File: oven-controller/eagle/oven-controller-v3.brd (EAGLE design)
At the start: 74.2 x 45.7 mm, 53 parts, among them Q1 FDV305N, Q2 FDV305N, Q3 FDV305N, Q4 FDV305N, U1 ARDUINO_SHIELDNOHOLES, U2 MAX31855, U3 MAX31855, U4 MAX31855, U5 MAX31855, U6 MAX31855

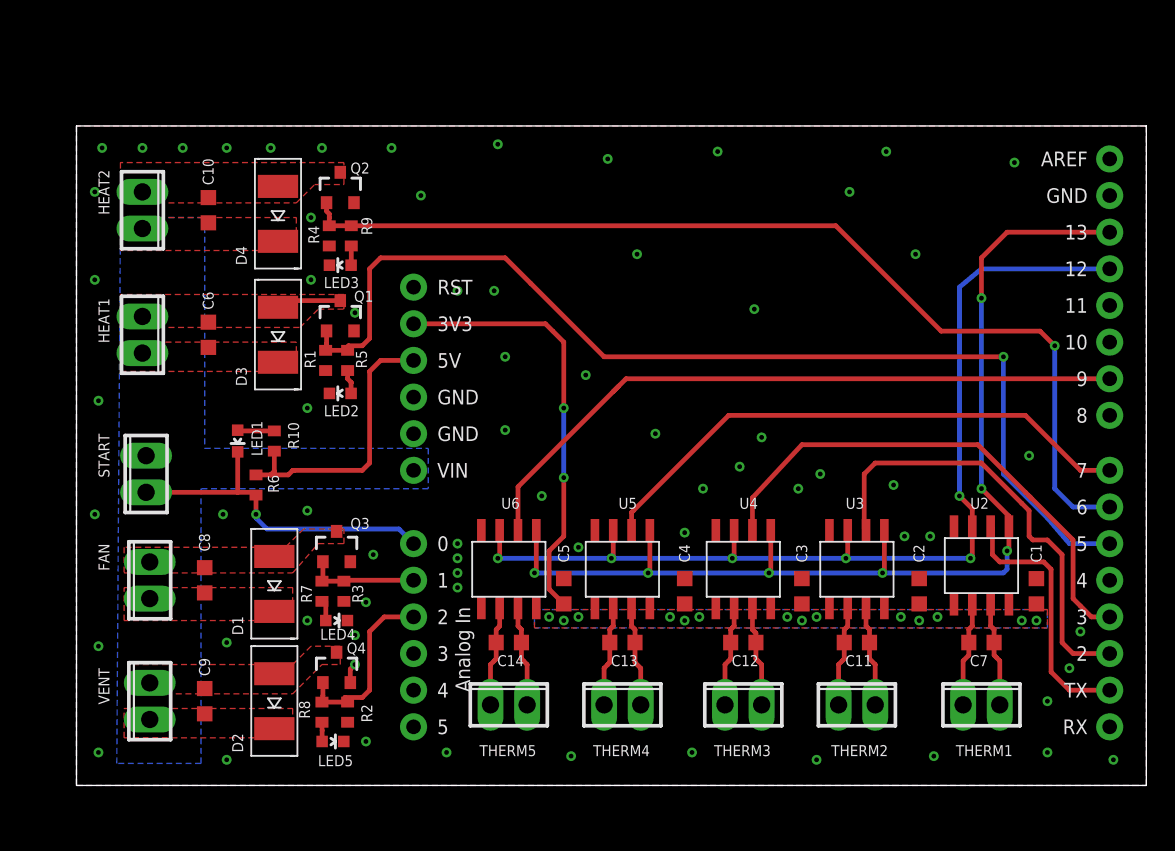
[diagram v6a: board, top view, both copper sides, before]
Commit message: Added level translators. Passes ERC, DRC. Needs review.
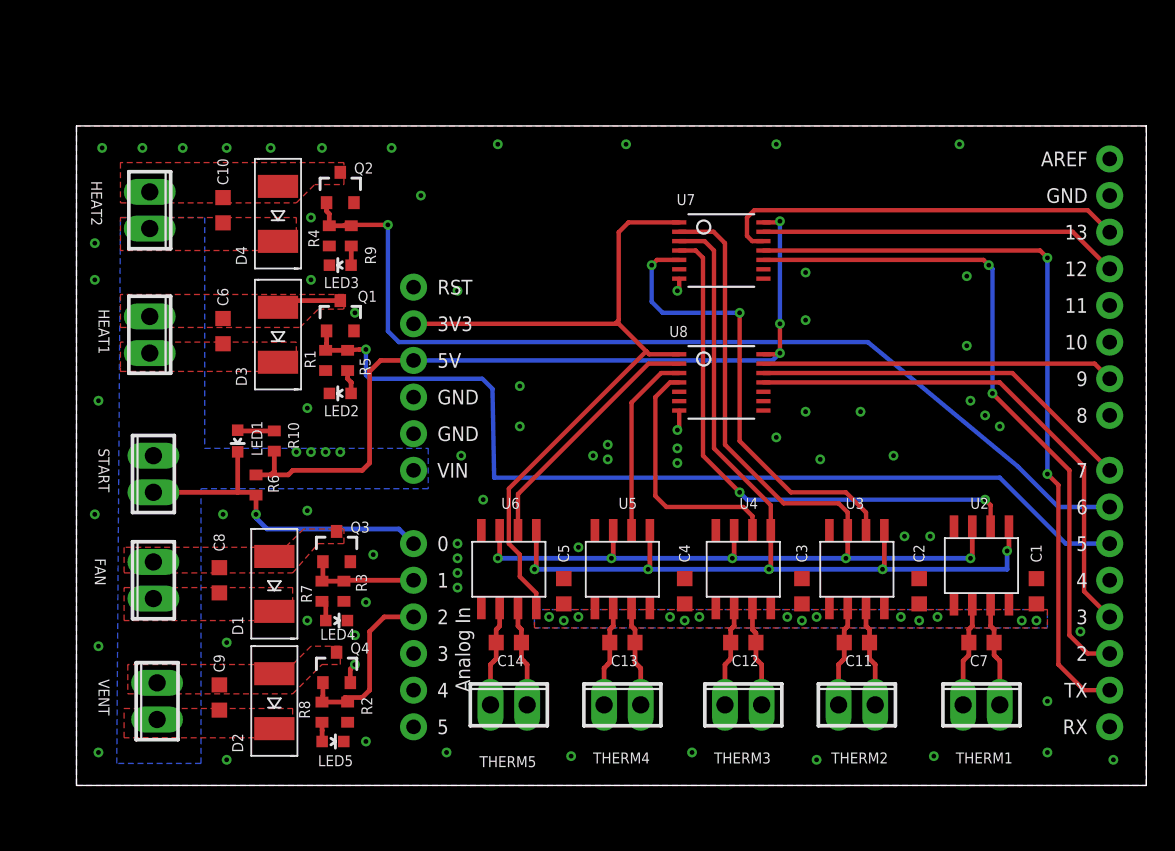
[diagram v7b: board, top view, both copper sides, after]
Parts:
- added U7, U8: (no value), SparkFun-DigitalIC:TSSOP14
- moved C9 1.05 mm to (9.91, 6.10)
- moved C6 1.05 mm to (10.2, 31.5)
- moved C10 1.02 mm to (10.2, 39.9)
- moved C8 1.02 mm to (9.91, 14.2)
- moved HEAT1 0.51 mm to (5.08, 31.2)
- moved HEAT2 0.51 mm to (5.08, 39.9)
- moved START 0.51 mm to (5.33, 21.6)
- moved VENT 0.51 mm to (5.59, 5.84)
- moved FAN 0.25 mm to (5.33, 14.2)
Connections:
- removed net SPI_CLK: U1.D13, U2.5, U3.5, U4.5, U5.5, U6.5
- removed net SPI_MISO: U1.D12, U2.7, U3.7, U4.7, U5.7, U6.7
- removed net THERM_!CS1: U1.TX, U2.6
- removed net THERM_!CS2: U1.D2, U3.6
- removed net THERM_!CS3: U1.D3, U4.6
- removed net THERM_!CS4: U1.D7, U5.6
- removed net THERM_!CS5: U1.D9, U6.6
- new net SPI_CLK_A: U2.5, U3.5, U4.5, U5.5, U6.5, U7.3
- new net SPI_CLK_B: U1.D13, U7.12
- new net SPI_MISO_A: U2.7, U3.7, U4.7, U5.7, U6.7, U7.2
- new net SPI_MISO_B: U1.D12, U7.13
- new net THERM_!CS1_A: U2.6, U7.4
- new net THERM_!CS1_B: U1.TX, U7.11
- new net THERM_!CS2_A: U3.6, U7.5
- new net THERM_!CS2_B: U1.D2, U7.10
- new net THERM_!CS3_A: U4.6, U8.4
- new net THERM_!CS3_B: U1.D3, U8.11
- new net THERM_!CS4_A: U5.6, U8.3
- new net THERM_!CS4_B: U1.D7, U8.12
- new net THERM_!CS5_A: U6.6, U8.2
- new net THERM_!CS5_B: U1.D9, U8.13
- net 3.3V: now also U7.1, U8.1
- net 5V: now also U7.14, U8.14
- net GND: now also U7.7, U8.7
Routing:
- net SPI_CLK: track 77.0 -> 0.00 mm, vias 7 -> 0
- net SPI_MISO_A: track 0.00 -> 72.2 mm, vias 0 -> 5
- net SPI_CLK_A: track 0.00 -> 71.5 mm, vias 0 -> 5
- net SPI_MISO: track 70.9 -> 0.00 mm, vias 6 -> 0
- net THERM_!CS1_B: track 0.00 -> 52.9 mm, vias 0 -> 2
- net THERM_!CS5: track 47.7 -> 0.00 mm
- net THERM_!CS2_B: track 0.00 -> 47.1 mm, vias 0 -> 2
- net THERM_!CS4: track 38.7 -> 0.00 mm
- net THERM_!CS1_A: track 0.00 -> 38.4 mm, vias 0 -> 2
- net 5V: track 19.7 -> 56.8 mm, vias 0 -> 3
- net THERM_!CS3: track 36.1 -> 0.00 mm
- net THERM_!CS3_B: track 0.00 -> 35.8 mm
- net THERM_!CS2_A: track 0.00 -> 31.9 mm, vias 0 -> 2
- net THERM_!CS2: track 31.4 -> 0.00 mm
- net SPI_CLK_B: track 0.00 -> 28.5 mm
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
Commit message: Added v3.1 update to oven board.
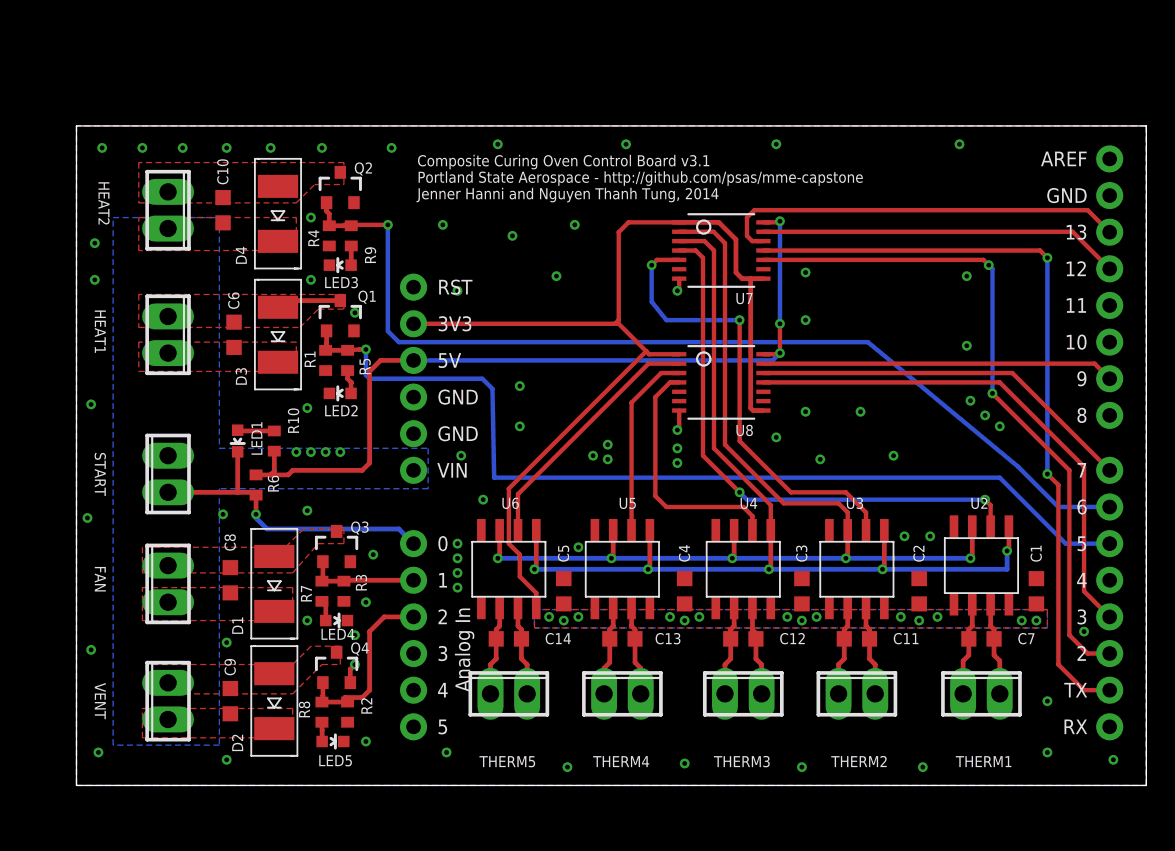
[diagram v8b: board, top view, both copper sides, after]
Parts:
- R10: value 1k -> 150
- U7, U8: value (none) -> TXB0104
- moved HEAT1 1.27 mm to (6.35, 31.2)
- moved HEAT2 1.27 mm to (6.35, 39.9)
- moved FAN 1.05 mm to (6.35, 14.0)
- moved START 1.02 mm to (6.35, 21.6)
- moved C6 0.80 mm to (10.9, 31.2)
- moved C9 0.80 mm to (10.7, 5.84)
- moved THERM1 0.76 mm to (62.7, 6.35)
- moved THERM2 0.76 mm to (54.1, 6.35)
- moved THERM3 0.76 mm to (46.2, 6.35)
- moved THERM4 0.76 mm to (37.8, 6.35)
- moved THERM5 0.76 mm to (30.0, 6.35)
- moved VENT 0.76 mm to (6.35, 5.84)
- moved C8 0.76 mm to (10.7, 14.2)
- moved C11 0.25 mm to (54.1, 10.2)
- moved C12 0.25 mm to (46.2, 10.2)
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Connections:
- net 3.3V: now also U7.8, U8.8
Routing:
- net 3.3V: track 52.8 -> 71.5 mm
- net !START: track 23.2 -> 22.2 mm
- net N$6: track 6.97 -> 6.21 mm
- net N$20: track 6.97 -> 6.21 mm
- net N$12: track 6.97 -> 6.21 mm
- net N$10: track 6.97 -> 6.21 mm
- net N$8: track 6.97 -> 6.21 mm
- net N$5: track 7.23 -> 6.46 mm
- net N$2: track 7.23 -> 6.46 mm
- net N$17: track 6.97 -> 6.21 mm
- net N$15: track 6.97 -> 6.21 mm
- net N$13: track 6.97 -> 6.21 mm
- net GND: vias 72 -> 75
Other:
- board text added: "Composite Curing Oven Control Board v3.1 Portland State Aerospace - http://github.com/psas/mme-capstone Jenner Hanni and Nguyen Thanh Tung, 2014"
